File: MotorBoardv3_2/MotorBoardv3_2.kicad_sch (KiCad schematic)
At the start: 79 parts, among them J1 Bump0, J11 GP2Y0A41SK0F, J12 GP2Y0A41SK0F, J13 GP2Y0A41SK0F, J15 7.2, J16 LP5.0, J17 ELA, J18 ERA, J19 Voltage Display Port, J2 Bump1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

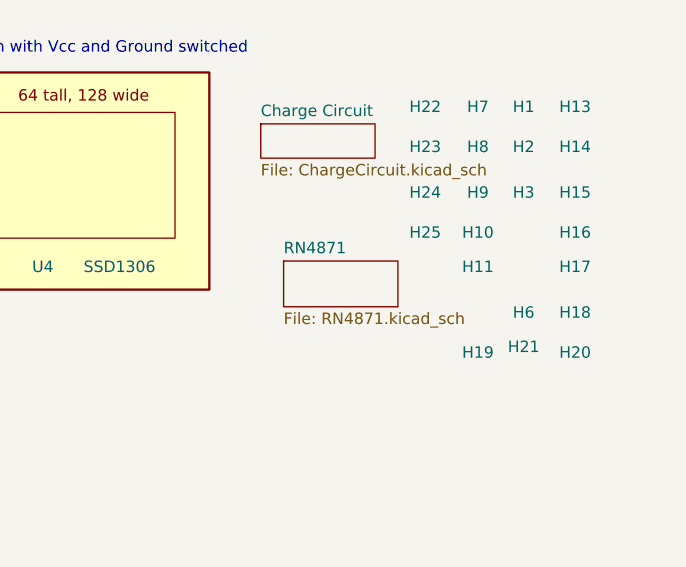
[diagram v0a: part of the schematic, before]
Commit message: Removed old bluetooth module from schematic and layout
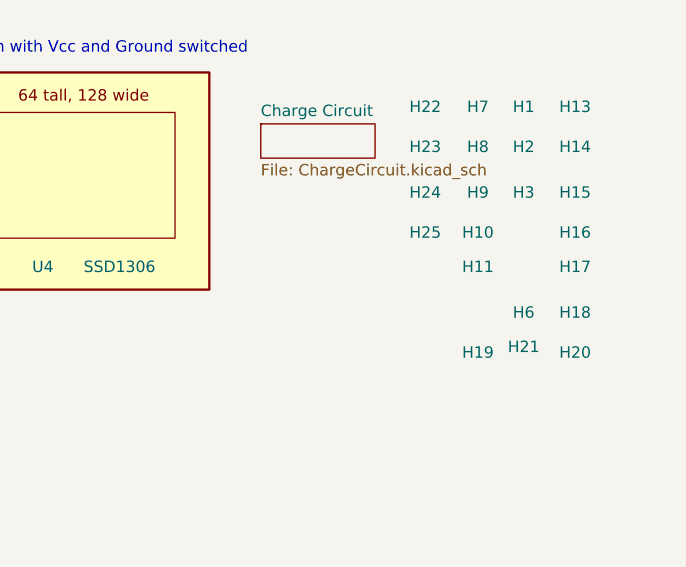
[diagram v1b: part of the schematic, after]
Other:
- removed sheet RN4871
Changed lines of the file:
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@@
 	(label "ELB"
 		(at 133.35 97.155 0)
+		(fields_autoplaced yes)
 		(effects
 			(font
@@
 	(label "ELA"
 		(at 138.43 93.345 0)
+		(fields_autoplaced yes)
 		(effects
 			(font
@@
 	(label "ERA"
 		(at 183.515 93.345 0)
+		(fields_autoplaced yes)
 		(effects
 			(font
@@
 	(label "LP3_3"
 		(at 20.32 24.13 0)
+		(fields_autoplaced yes)
 		(effects
 			(font
@@
 	(label "ERB"
 		(at 183.515 97.155 0)
+		(fields_autoplaced yes)
 		(effects
 			(font
@@
 	(label "VBUS"
 		(at 48.895 19.05 0)
+		(fields_autoplaced yes)
 		(effects
 			(font
@@
 				)
 			)
-		)
-	)
-	(sheet
-		(at 246.38 152.4)
-		(size 12.7 5.08)
-		(fields_autoplaced yes)
-		(stroke
-			(width 0.1524)
-			(type solid)
-		)
-		(fill
-			(color 0 0 0 0.0000)
-		)
-		(property "Sheetname" "RN4871"
-			(at 246.38 151.6884 0)
-			(effects
-				(font
-					(size 1.27 1.27)
-				)
-				(justify left bottom)
-			)
-		)
-		(property "Sheetfile" "RN4871.kicad_sch"
-			(at 246.38 158.0646 0)
-			(effects
-				(font
-					(size 1.27 1.27)
-				)
-				(justify left top)
-			)
-		)
-		(instances
-			(project "MotorBoardv3_2"
-				(path "/69b823fd-c065-40ff-9bb9-c5835555f3eb"
-					(page "2")
-				)
-			)

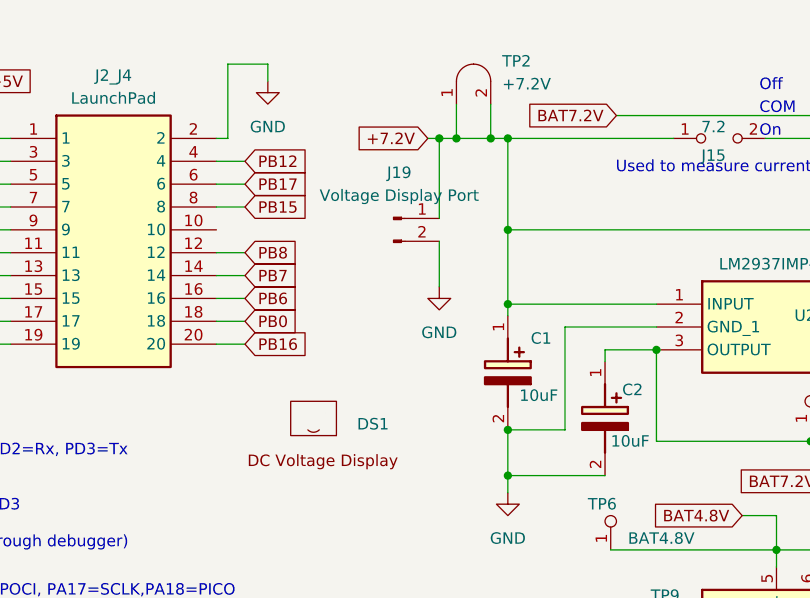
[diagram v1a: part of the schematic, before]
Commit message: added voltmeter button to schematic
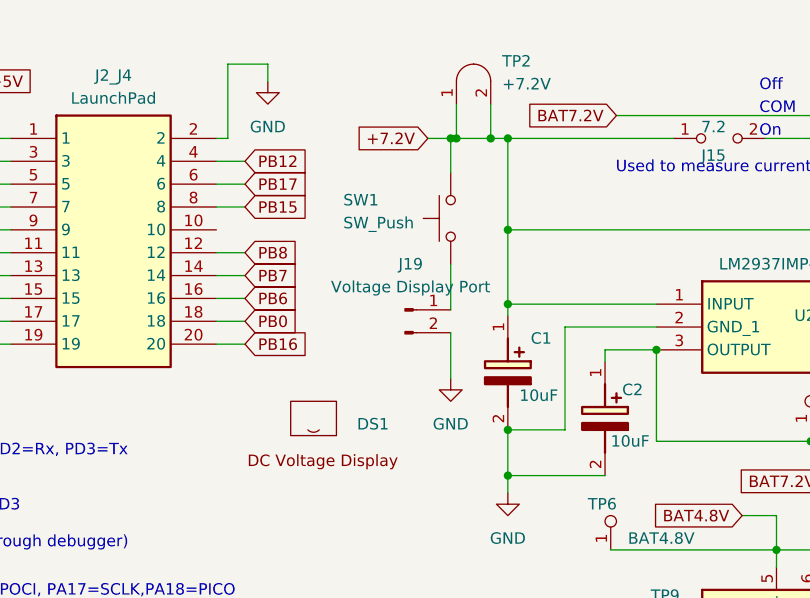
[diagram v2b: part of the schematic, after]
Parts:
- added SW1: SW_Push, symbol Switch:SW_Push
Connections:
- net +7.2V: now also SW1.2; no longer J19.1 (Pin_1)
- new net: J19.1 (Pin_1), SW1.1
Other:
- moved on the sheet: J19
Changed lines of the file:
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@@
 	)
 	(junction
-		(at 118.11 25.4)
-		(diameter 0)
-		(color 0 0 0 0)
-	)
-	(junction
 		(at 25.4 177.8)
 		(diameter 0)
@@
 	)
 	(junction
+		(at 119.38 25.4)
+		(diameter 0)
+		(color 0 0 0 0)
+	)
+	(junction
 		(at 213.36 53.34)
 		(diameter 0)
@@
 	(wire
 		(pts
-			(xy 116.84 25.4) (xy 118.11 25.4)
+			(xy 116.84 25.4) (xy 119.38 25.4)
 		)
 		(stroke
@@
 	(wire
 		(pts
-			(xy 118.11 25.4) (xy 118.11 34.29)
-		)
-		(stroke
-			(width 0)
-			(type default)
-		)
-	)
-	(wire
-		(pts
 			(xy 153.67 140.97) (xy 153.67 139.065)
 		)
@@
 	(wire
 		(pts
-			(xy 118.11 36.83) (xy 118.11 41.91)
+			(xy 119.38 46.99) (xy 119.38 52.07)
+		)
+		(stroke
+			(width 0)
+			(type default)
+		)
+	)
+	(wire
+		(pts
+			(xy 119.38 25.4) (xy 119.38 29.21)
 		)
 		(stroke
@@
 	(wire
 		(pts
+			(xy 119.38 25.4) (xy 120.015 25.4)
+		)
+		(stroke
+			(width 0)
+			(type default)
+		)
+	)
+	(wire
+		(pts
 			(xy 22.86 45.72) (xy 26.035 45.72)
 		)
@@
 	(wire
 		(pts
-			(xy 118.11 25.4) (xy 120.015 25.4)
-		)
-		(stroke
-			(width 0)
-			(type default)
-		)
-	)
-	(wire
-		(pts
 			(xy 127.635 189.23) (xy 127.635 191.135)
 		)
@@
 	(wire
 		(pts
+			(xy 119.38 39.37) (xy 119.38 44.45)
+		)
+		(stroke
+			(width 0)
+			(type default)
+		)
+	)
+	(wire
+		(pts
 			(xy 262.255 97.155) (xy 265.43 97.155)
 		)
@@
 	(symbol
 		(lib_id "power:GND")
-		(at 118.11 41.91 0)
+		(at 119.38 52.07 0)
 		(unit 1)
 		(exclude_from_sim no)
@@
 		(fields_autoplaced yes)
 		(property "Reference" "#PWR021"
-			(at 118.11 48.26 0)
+			(at 119.38 58.42 0)
 			(effects
 				(font
@@
 		)
 		(property "Value" "GND"
-			(at 118.11 46.99 0)
+			(at 119.38 57.15 0)
 			(effects
 				(font
@@
 		)
 		(property "Footprint" ""
-			(at 118.11 41.91 0)
+			(at 119.38 52.07 0)
 			(effects
 				(font
@@
 		)
 		(property "Datasheet" ""
-			(at 118.11 41.91 0)
+			(at 119.38 52.07 0)
 			(effects
 				(font
@@
 		)
 		(property "Description" "Power symbol creates a global label with name \"GND\" , ground"
-			(at 118.11 41.91 0)
+			(at 119.38 52.07 0)
 			(effects
 				(font
@@
 	)
 	(symbol
+		(lib_id "Switch:SW_Push")
+		(at 119.38 34.29 90)
+		(unit 1)
+		(exclude_from_sim no)
+		(in_bom yes)
+		(on_board yes)
+		(dnp no)
+		(property "Reference" "SW1"
+			(at 107.442 32.258 90)
+			(effects
+				(font
+					(size 1.27 1.27)
+				)
+				(justify right)
+			)
+		)
+		(property "Value" "SW_Push"
+			(at 107.442 34.798 90)
+			(effects
+				(font
+					(size 1.27 1.27)
+				)
+				(justify right)
+			)
+		)
+		(property "Footprint" ""
+			(at 114.3 34.29 0)
+			(effects
+				(font
+					(size 1.27 1.27)
+				)
+				(hide yes)
+			)
+		)
+		(property "Datasheet" "~"
+			(at 114.3 34.29 0)
+			(effects
+				(font
+					(size 1.27 1.27)
+				)
+				(hide yes)
+			)
+		)
+		(property "Description" "Push button switch, generic, two pins"
+			(at 119.38 34.29 0)
+			(effects
+				(font
+					(size 1.27 1.27)
+				)
+				(hide yes)
+			)
+		)
+		(pin "1"
+		)
+		(pin "2"
+		)
+		(instances
+			(project ""
+				(path "/69b823fd-c065-40ff-9bb9-c5835555f3eb"
+					(reference "SW1")
+					(unit 1)
+				)
+			)
+		)
+	)
+	(symbol
 		(lib_id "RSLK2:TAJB106K020RNJ")
 		(at 153.67 140.97 270)
@@
 	(symbol
 		(lib_id "Connector:Conn_01x02_Pin")
-		(at 113.03 34.29 0)
+		(at 114.3 44.45 0)
 		(unit 1)
 		(exclude_from_sim no)
@@
 		(fields_autoplaced yes)
 		(property "Reference" "J19"
-			(at 113.665 29.21 0)
+			(at 114.935 39.37 0)
 			(effects
 				(font
@@
 		)
 		(property "Value" "Voltage Display Port"
-			(at 113.665 31.75 0)
+			(at 114.935 41.91 0)
 			(effects
 				(font
@@
 		)
 		(property "Footprint" "Connector_Wire:SolderWire-0.15sqmm_1x02_P4mm_D0.5mm_OD1.5mm_Relief"
-			(at 113.03 34.29 0)
+			(at 114.3 44.45 0)
 			(effects
 				(font
@@
 		)
 		(property "Datasheet" "~"
-			(at 113.03 34.29 0)
+			(at 114.3 44.45 0)
 			(effects
 				(font
@@
 		)
 		(property "Description" "Generic connector, single row, 01x02, script generated"
-			(at 113.03 34.29 0)
+			(at 114.3 44.45 0)
 			(effects
 				(font

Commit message: added a possible footprint for button
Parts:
- SW1: footprint (none) -> Button_Switch_THT:SW_CW_GPTS203211B
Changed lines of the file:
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@@
 			)
 		)
-		(property "Footprint" ""
+		(property "Footprint" "Button_Switch_THT:SW_CW_GPTS203211B"
 			(at 114.3 34.29 0)
 			(effects

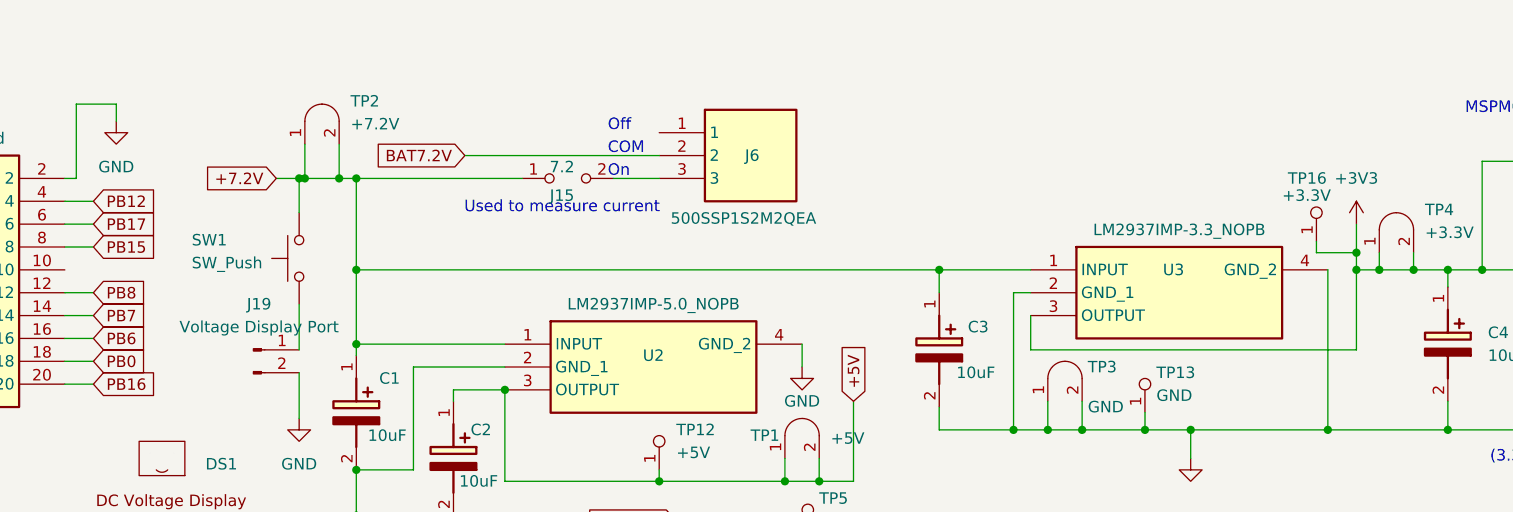
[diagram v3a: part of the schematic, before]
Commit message: added button for DC Display
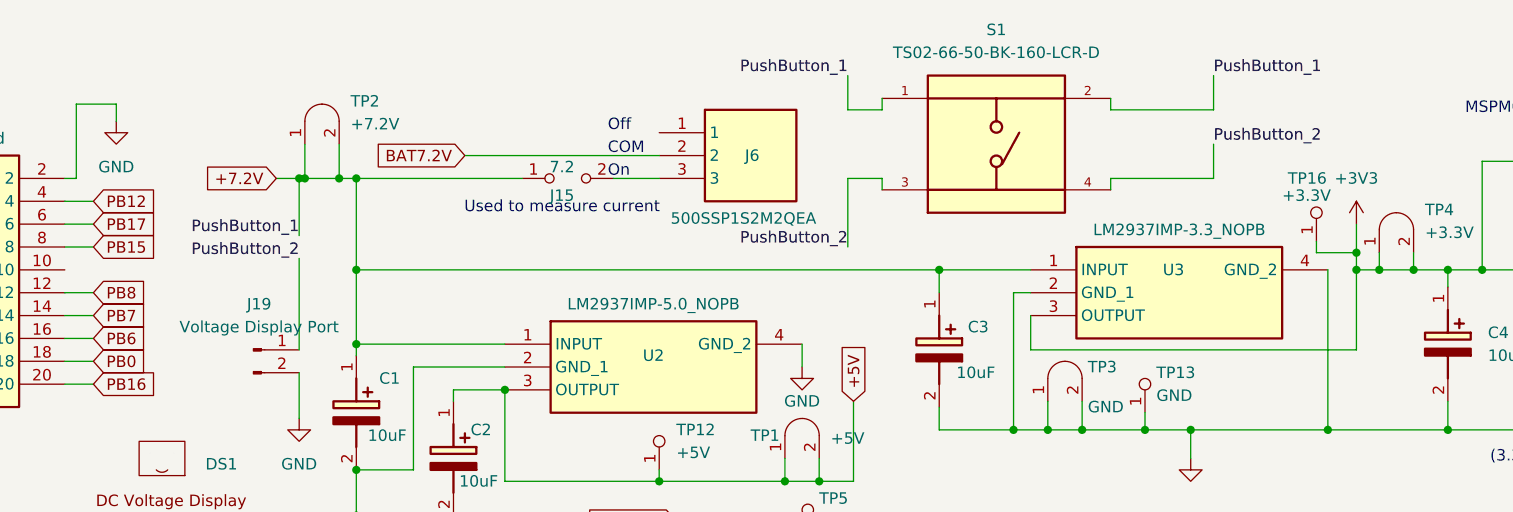
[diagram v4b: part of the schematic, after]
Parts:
- removed SW1: SW_Push, Button_Switch_THT:SW_CW_GPTS203211B, symbol Switch:SW_Push
- added S1: TS02-66-50-BK-160-LCR-D, RSLK2:SW_TS02-66-50-BK-160-LCR-D, symbol RSLK2:TS02-66-50-BK-160-LCR-D
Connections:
- net +7.2V: now also S1.1, S1.2
- net PushButton_2: now reaches J19.1 (Pin_1)
- net PushButton_2: now also S1.3, S1.4
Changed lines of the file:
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@@
 	(wire
 		(pts
+			(xy 209.55 25.4) (xy 209.55 26.67)
+		)
+		(stroke
+			(width 0)
+			(type default)
+		)
+	)
+	(wire
+		(pts
 			(xy 132.08 46.355) (xy 132.08 57.785)
 		)
@@
 	(wire
 		(pts
+			(xy 180.34 13.97) (xy 180.34 17.78)
+		)
+		(stroke
+			(width 0)
+			(type default)
+		)
+	)
+	(wire
+		(pts
 			(xy 25.4 177.8) (xy 40.64 177.8)
 		)
@@
 	(wire
 		(pts
+			(xy 184.15 17.78) (xy 184.15 16.51)
+		)
+		(stroke
+			(width 0)
+			(type default)
+		)
+	)
+	(wire
+		(pts
 			(xy 147.955 161.925) (xy 147.955 164.465)
 		)
@@
 	(wire
 		(pts
+			(xy 220.98 25.4) (xy 209.55 25.4)
+		)
+		(stroke
+			(width 0)
+			(type default)
+		)
+	)
+	(wire
+		(pts
 			(xy 180.34 93.345) (xy 203.835 93.345)
 		)
@@
 	(wire
 		(pts
+			(xy 180.34 25.4) (xy 184.15 25.4)
+		)
+		(stroke
+			(width 0)
+			(type default)
+		)
+	)
+	(wire
+		(pts
 			(xy 155.575 71.12) (xy 168.91 71.12)
 		)
@@
 	(wire
 		(pts
+			(xy 220.98 21.59) (xy 220.98 25.4)
+		)
+		(stroke
+			(width 0)
+			(type default)
+		)
+	)
+	(wire
+		(pts
 			(xy 23.495 134.62) (xy 40.64 134.62)
 		)
@@
 	(wire
 		(pts
+			(xy 119.38 25.4) (xy 119.38 31.75)
+		)
+		(stroke
+			(width 0)
+			(type default)
+		)
+	)
+	(wire
+		(pts
 			(xy 67.945 33.02) (xy 70.485 33.02)
 		)
@@
 	(wire
 		(pts
+			(xy 220.98 13.97) (xy 220.98 17.78)
+		)
+		(stroke
+			(width 0)
+			(type default)
+		)
+	)
+	(wire
+		(pts
 			(xy 243.205 33.655) (xy 243.205 35.56)
 		)
@@
 	(wire
 		(pts
-			(xy 119.38 25.4) (xy 119.38 29.21)
-		)
-		(stroke
-			(width 0)
-			(type default)
-		)
-	)
-	(wire
-		(pts
 			(xy 99.06 164.465) (xy 112.395 164.465)
 		)
@@
 	(wire
 		(pts
+			(xy 220.98 17.78) (xy 209.55 17.78)
+		)
+		(stroke
+			(width 0)
+			(type default)
+		)
+	)
+	(wire
+		(pts
 			(xy 198.12 144.78) (xy 198.12 142.24)
 		)
@@
 	(wire
 		(pts
+			(xy 209.55 17.78) (xy 209.55 16.51)
+		)
+		(stroke
+			(width 0)
+			(type default)
+		)
+	)
+	(wire
+		(pts
 			(xy 183.515 80.645) (xy 183.515 81.915)
 		)
@@
 	(wire
 		(pts
+			(xy 184.15 25.4) (xy 184.15 26.67)
+		)
+		(stroke
+			(width 0)
+			(type default)
+		)
+	)
+	(wire
+		(pts
 			(xy 200.66 139.7) (xy 202.565 139.7)
 		)
@@
 	(wire
 		(pts
+			(xy 180.34 17.78) (xy 184.15 17.78)
+		)
+		(stroke
+			(width 0)
+			(type default)
+		)
+	)
+	(wire
+		(pts
 			(xy 200.66 44.45) (xy 236.855 44.45)
 		)
@@
 	(wire
 		(pts
+			(xy 180.34 25.4) (xy 180.34 33.02)
+		)
+		(stroke
+			(width 0)
+			(type default)
+		)
+	)
+	(wire
+		(pts
 			(xy 202.565 142.24) (xy 200.66 142.24)
 		)
@@
 	(wire
 		(pts
-			(xy 119.38 39.37) (xy 119.38 44.45)
+			(xy 119.38 34.29) (xy 119.38 44.45)
 		)
 		(stroke
@@
 	(label "ELB"
 		(at 133.35 97.155 0)
-		(fields_autoplaced yes)
 		(effects
 			(font
@@
 		)
 	)
+	(label "PushButton_1"
+		(at 180.34 13.97 180)
+		(effects
+			(font
+				(size 1.27 1.27)
+			)
+			(justify right bottom)
+		)
+	)
+	(label "PushButton_2"
+		(at 180.34 33.02 180)
+		(effects
+			(font
+				(size 1.27 1.27)
+			)
+			(justify right bottom)
+		)
+	)
 	(label "ELA"
 		(at 138.43 93.345 0)
-		(fields_autoplaced yes)
 		(effects
 			(font
@@
 	(label "ERA"
 		(at 183.515 93.345 0)
-		(fields_autoplaced yes)
+		(effects
+			(font
+				(size 1.27 1.27)
+			)
+			(justify left bottom)
+		)
+	)
+	(label "PushButton_1"
+		(at 220.98 13.97 0)
 		(effects
 			(font
@@
 	(label "LP3_3"
 		(at 20.32 24.13 0)
-		(fields_autoplaced yes)
+		(effects
+			(font
+				(size 1.27 1.27)
+			)
+			(justify left bottom)
+		)
+	)
+	(label "PushButton_2"
+		(at 220.98 21.59 0)
 		(effects
 			(font
@@
 	(label "ERB"
 		(at 183.515 97.155 0)
-		(fields_autoplaced yes)
 		(effects
 			(font
@@
 		)
 	)
+	(label "PushButton_2"
+		(at 119.38 34.29 180)
+		(effects
+			(font
+				(size 1.27 1.27)
+			)
+			(justify right bottom)
+		)
+	)
 	(label "VBUS"
 		(at 48.895 19.05 0)
-		(fields_autoplaced yes)
 		(effects
 			(font
@@
 		)
 	)
+	(label "PushButton_1"
+		(at 119.38 31.75 180)
+		(effects
+			(font
+				(size 1.27 1.27)
+			)
+			(justify right bottom)
+		)
+	)
 	(global_label "PA26"
 		(shape input)
@@
 	)
 	(symbol
+		(lib_id "RSLK2:TS02-66-50-BK-160-LCR-D")
+		(at 196.85 21.59 0)
+		(unit 1)
+		(exclude_from_sim no)
+		(in_bom yes)
+		(on_board yes)
+		(dnp no)
+		(fields_autoplaced yes)
+		(property "Reference" "S1"
+			(at 196.85 8.89 0)
+			(effects
+				(font
+					(size 1.27 1.27)
+				)
+			)
+		)
+		(property "Value" "TS02-66-50-BK-160-LCR-D"
+			(at 196.85 11.43 0)
+			(effects
+				(font
+					(size 1.27 1.27)
+				)
+			)
+		)
+		(property "Footprint" "RSLK2:SW_TS02-66-50-BK-160-LCR-D"
+			(at 196.85 21.59 0)
+			(effects
+				(font
+					(size 1.27 1.27)
+				)
+				(justify bottom)
+				(hide yes)
+			)
+		)
+		(property "Datasheet" ""
+			(at 196.85 21.59 0)
+			(effects
+				(font
+					(size 1.27 1.27)
+				)
+				(hide yes)
+			)
+		)
+		(property "Description" ""
+			(at 196.85 21.59 0)
+			(effects
+				(font
+					(size 1.27 1.27)
+				)
+				(hide yes)
+			)
+		)
+		(property "PARTREV" "1.0"
+			(at 196.85 21.59 0)
+			(effects
+				(font
+					(size 1.27 1.27)
+				)
+				(justify bottom)
+				(hide yes)
+			)
+		)
+		(property "MANUFACTURER" "CUI Devices"
+			(at 196.85 21.59 0)
+			(effects
+				(font
+					(size 1.27 1.27)
+				)
+				(justify bottom)
+				(hide yes)
+			)
+		)
+		(property "STANDARD" "Manufacturer Recommendations"
+			(at 196.85 21.59 0)
+			(effects
+				(font
+					(size 1.27 1.27)
+				)
+				(justify bottom)
+				(hide yes)
+			)
+		)
+		(pin "3"
+		)
+		(pin "1"
+		)
+		(pin "2"
+		)
+		(pin "4"
+		)
+		(instances
+			(project ""
+				(path "/69b823fd-c065-40ff-9bb9-c5835555f3eb"
+					(reference "S1")
+					(unit 1)
+				)
+			)
+		)
+	)
+	(symbol
 		(lib_id "power:GND")
 		(at 127.635 191.135 0)
@@
 					(unit 1)
 				)
-			)
-		)
-	)
-	(symbol
-		(lib_id "Switch:SW_Push")
-		(at 119.38 34.29 90)
-		(unit 1)
-		(exclude_from_sim no)
-		(in_bom yes)
-		(on_board yes)
-		(dnp no)
-		(property "Reference" "SW1"
-			(at 107.442 32.258 90)
-			(effects
-				(font
-					(size 1.27 1.27)
-				)
-				(justify right)
-			)
-		)
-		(property "Value" "SW_Push"
-			(at 107.442 34.798 90)
-			(effects
-				(font
-					(size 1.27 1.27)
-				)
-				(justify right)
-			)
-		)
-		(property "Footprint" "Button_Switch_THT:SW_CW_GPTS203211B"
-			(at 114.3 34.29 0)
-			(effects
-				(font
-					(size 1.27 1.27)
-				)
-				(hide yes)
-			)
-		)
-		(property "Datasheet" "~"
-			(at 114.3 34.29 0)
-			(effects
-				(font
-					(size 1.27 1.27)
-				)
-				(hide yes)
-			)
-		)
-		(property "Description" "Push button switch, generic, two pins"
-			(at 119.38 34.29 0)
-			(effects
-				(font
-					(size 1.27 1.27)
-				)
-				(hide yes)
-			)
-		)
-		(pin "1"
-		)
-		(pin "2"
-		)
-		(instances
-			(project ""
-				(path "/69b823fd-c065-40ff-9bb9-c5835555f3eb"
-					(reference "SW1")
-					(unit 1)
-				)
